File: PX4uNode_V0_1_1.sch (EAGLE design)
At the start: 129 parts, among them M3_MOUNT1101 MOUNT-HOLE3.1MM, M3_MOUNT1102 MOUNT-HOLE3.1MM, M3_MOUNT1103 MOUNT-HOLE3.1MM, M3_MOUNT1104 MOUNT-HOLE3.1MM, U101 STM32F4X7VX, U401 MAX3051, U402 MAX3051, X101 3.2x2.5 mm / 24 MHz / 15 ppm

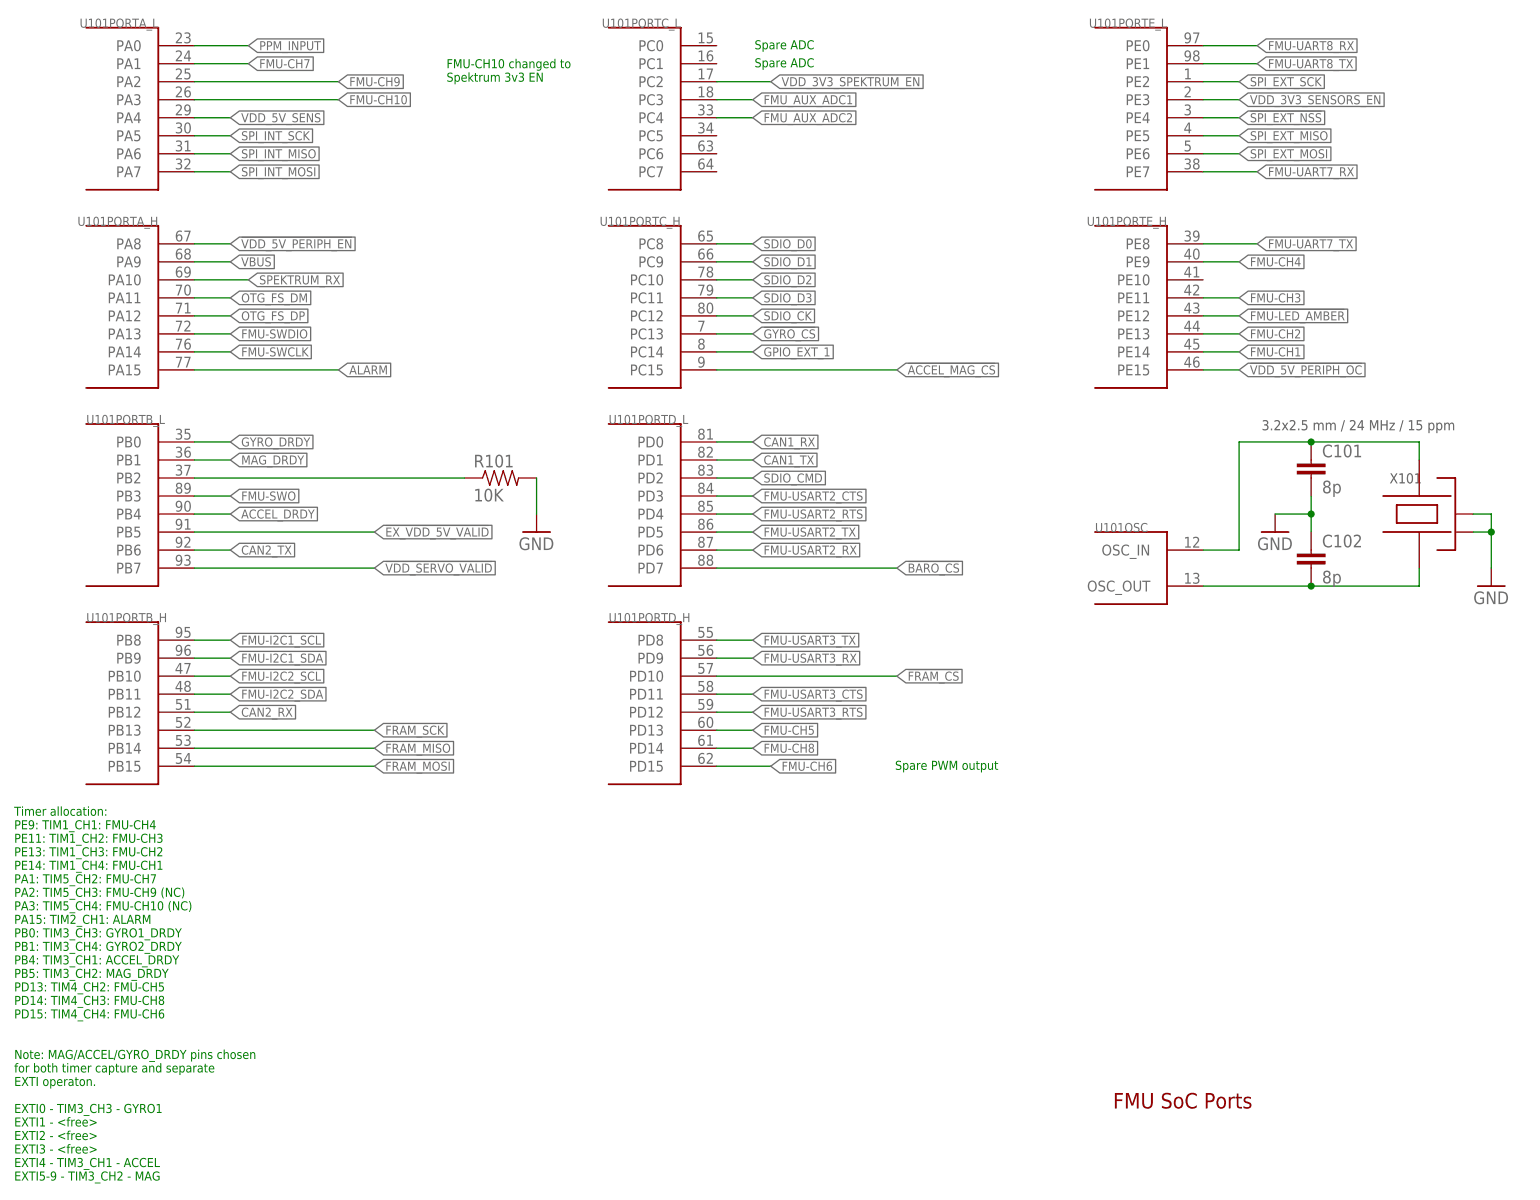
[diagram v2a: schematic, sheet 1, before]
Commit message: uNode - More pullup resistor placed
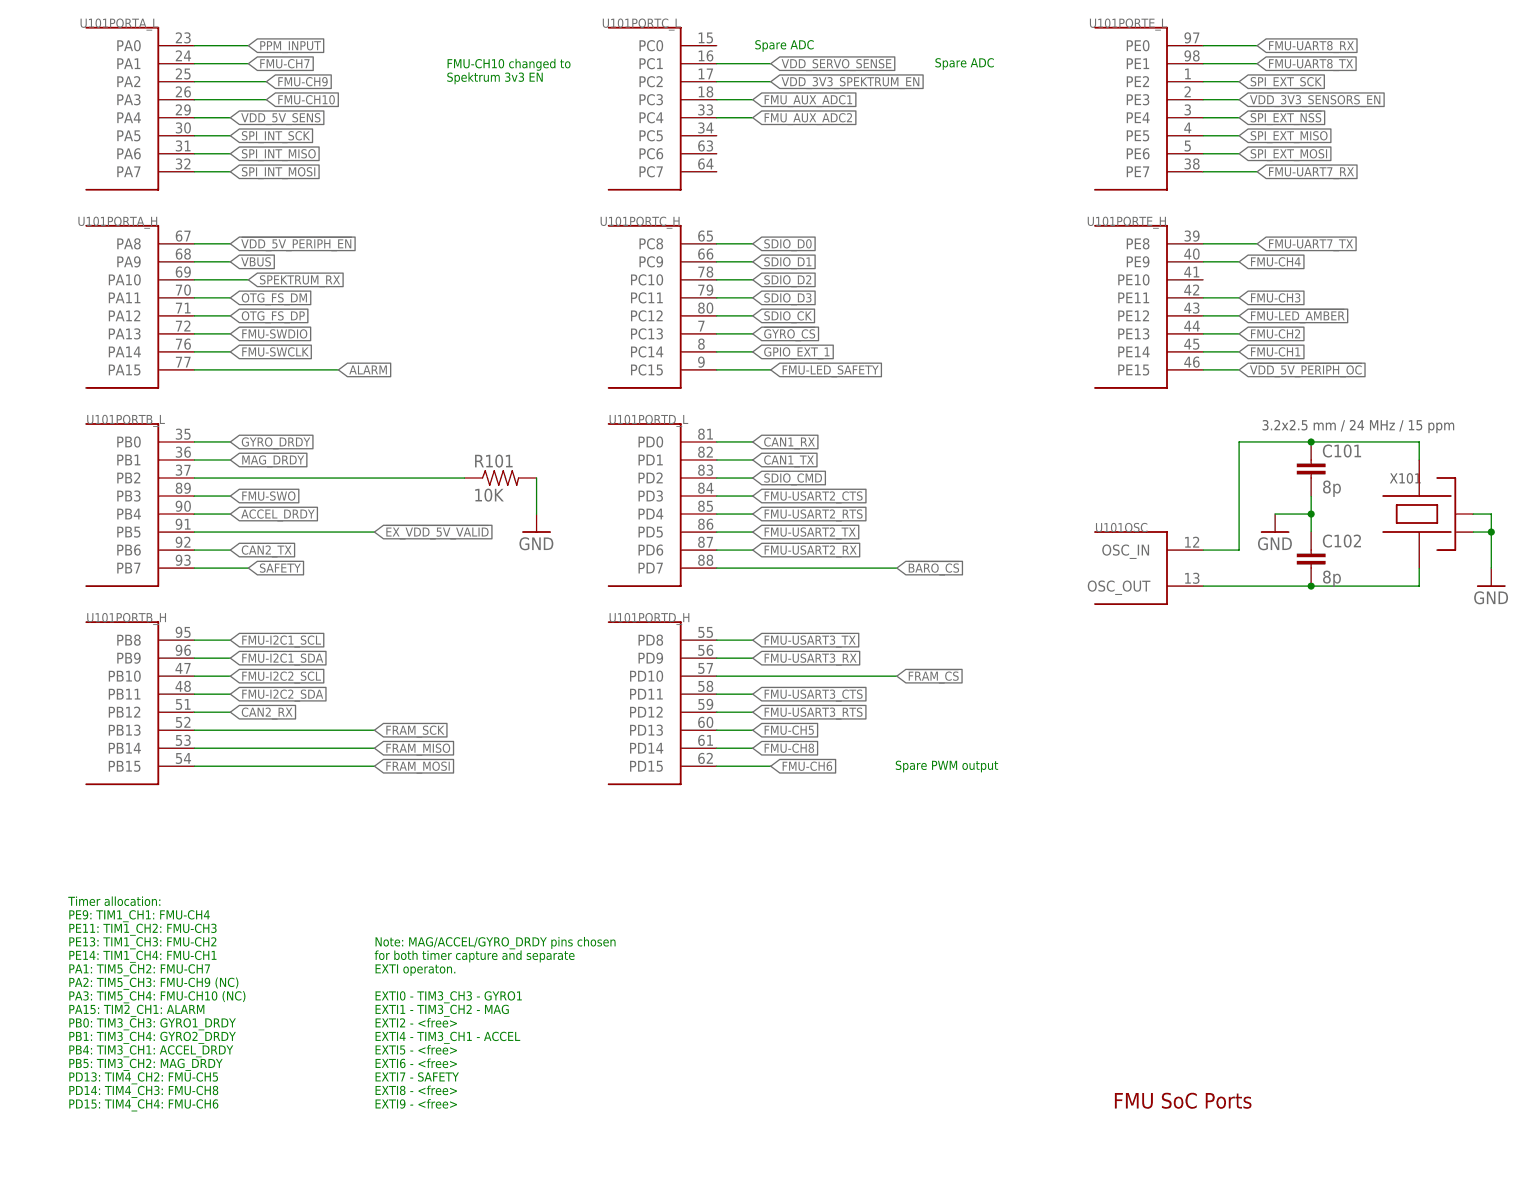
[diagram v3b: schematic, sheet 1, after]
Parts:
- added R1: 10K, pixhawk2:RESISTOR0402-RES
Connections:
- removed net !ACCEL_MAG_CS: U101PORTC_H.PC15
- removed net !VDD_SERVO_VALID: U101PORTB_L.PB7
- removed net VDD_SERVO_SENS: R902.1, R903.2
- new net VDD_SERVO_SENSE: R902.1, R903.2, U101PORTC_L.PC1
- net !VDD_5V_PERIPH_OC: now also R1.2
- net FMU-LED_SAFETY: now also U101PORTC_H.PC15
- net FMU-VDD_3V3: now also R1.1, R705.1
- net SAFETY: now also U101PORTB_L.PB7
- net VDD_5V: no longer R705.1
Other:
- note added: "Note: MAG/ACCEL/GYRO_DRDY pins chosen for both timer capture and separate EXTI operaton. EXTI0 - TIM3_CH3 - GYRO1 EXTI1 - TIM3_CH2 - MAG EXTI2 - <free> EXTI4 - TIM3_CH1 - ACCEL EXTI5 - <free> EXTI6 - <free> EXTI7 - SAFETY EXTI8 - <free> EXTI9 - <free>"
- note removed: "Note: MAG/ACCEL/GYRO_DRDY pins chosen for both timer capture and separate EXTI operaton. EXTI0 - TIM3_CH3 - GYRO1 EXTI1 - <free> EXTI2 - <free> EXTI3 - <free> EXTI4 - TIM3_CH1 - ACCEL EXTI5-9 - TIM3_CH2 - MAG"
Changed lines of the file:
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@@
 <part name="GND19" library="pixhawk2" deviceset="GND" device=""/>
 <part name="U$3" library="PX4lite" deviceset="NUF2042XV6" device=""/>
+<part name="R1" library="pixhawk2" deviceset="RESISTOR" device="0402-RES" value="10K">
+<attribute name="PARTNO" value="RC0402FR-0710KL"/>
+</part>
 </parts>
 <sheets>
@@
 <text x="162.56" y="15.24" size="2.1844" layer="94" font="vector" ratio="10">FMU SoC Ports
 </text>
-<text x="7.62" y="5.08" size="1.27" layer="91">Note: MAG/ACCEL/GYRO_DRDY pins chosen
+<text x="58.42" y="15.24" size="1.27" layer="91">Note: MAG/ACCEL/GYRO_DRDY pins chosen
 for both timer capture and separate
 EXTI operaton.
 EXTI0 - TIM3_CH3 - GYRO1
-EXTI1 - &lt;free&gt;
+EXTI1 - TIM3_CH2 - MAG
 EXTI2 - &lt;free&gt;
-EXTI3 - &lt;free&gt;
 EXTI4 - TIM3_CH1 - ACCEL
-EXTI5-9 - TIM3_CH2 - MAG
+EXTI5 - &lt;free&gt;
+EXTI6 - &lt;free&gt;
+EXTI7 - SAFETY
+EXTI8 - &lt;free&gt;
+EXTI9 - &lt;free&gt;
 </text>
-<text x="7.62" y="27.94" size="1.27" layer="91">Timer allocation:
+<text x="15.24" y="15.24" size="1.27" layer="91">Timer allocation:
 PE9: TIM1_CH1: FMU-CH4
 PE11: TIM1_CH2: FMU-CH3
@@
 <text x="131.826" y="62.992" size="1.27" layer="91">Spare PWM output</text>
 <text x="112.014" y="164.592" size="1.27" layer="91">Spare ADC</text>
-<text x="112.014" y="162.052" size="1.27" layer="91">Spare ADC</text>
+<text x="137.414" y="162.052" size="1.27" layer="91">Spare ADC</text>
 <text x="68.58" y="160.02" size="1.27" layer="91">FMU-CH10 changed to
 Spektrum 3v3 EN</text>
@@
 </segment>
 </net>
-<net name="!ACCEL_MAG_CS" class="0">
+<net name="FMU-LED_SAFETY" class="0">
 <segment>
 <pinref part="U101" gate="PORTC_H" pin="PC15"/>
-<wire x1="106.68" y1="119.38" x2="132.08" y2="119.38" width="0.1524" layer="91"/>
-<label x="132.08" y="119.38" size="1.27" layer="95" xref="yes"/>
+<wire x1="106.68" y1="119.38" x2="114.3" y2="119.38" width="0.1524" layer="91"/>
+<label x="114.3" y="119.38" size="1.27" layer="95" xref="yes"/>
 </segment>
 </net>
@@
 </segment>
 </net>
-<net name="!VDD_SERVO_VALID" class="0">
-<segment>
-<pinref part="U101" gate="PORTB_L" pin="PB7"/>
-<wire x1="33.02" y1="91.44" x2="58.42" y2="91.44" width="0.1524" layer="91"/>
-<label x="58.42" y="91.44" size="1.27" layer="95" xref="yes"/>
-</segment>
-</net>
 <net name="GPIO_EXT_1" class="0">
 <segment>
@@
 <segment>
 <pinref part="U101" gate="PORTA_L" pin="PA2"/>
-<wire x1="33.02" y1="160.02" x2="53.34" y2="160.02" width="0.1524" layer="91"/>
-<label x="53.34" y="160.02" size="1.27" layer="95" xref="yes"/>
+<wire x1="33.02" y1="160.02" x2="43.18" y2="160.02" width="0.1524" layer="91"/>
+<label x="43.18" y="160.02" size="1.27" layer="95" xref="yes"/>
 </segment>
 </net>
@@
 <segment>
 <pinref part="U101" gate="PORTA_L" pin="PA3"/>
-<wire x1="33.02" y1="157.48" x2="53.34" y2="157.48" width="0.1524" layer="91"/>
-<label x="53.34" y="157.48" size="1.27" layer="95" xref="yes"/>
+<wire x1="33.02" y1="157.48" x2="43.18" y2="157.48" width="0.1524" layer="91"/>
+<label x="43.18" y="157.48" size="1.27" layer="95" xref="yes"/>
+</segment>
+</net>
+<net name="SAFETY" class="0">
+<segment>
+<pinref part="U101" gate="PORTB_L" pin="PB7"/>
+<wire x1="33.02" y1="91.44" x2="40.64" y2="91.44" width="0.1524" layer="91"/>
+<label x="40.64" y="91.44" size="1.27" layer="95" xref="yes"/>
+</segment>
+</net>
+<net name="VDD_SERVO_SENSE" class="0">
+<segment>
+<pinref part="U101" gate="PORTC_L" pin="PC1"/>
+<wire x1="106.68" y1="162.56" x2="114.3" y2="162.56" width="0.1524" layer="91"/>
+<label x="114.3" y="162.56" size="1.27" layer="95" xref="yes"/>
 </segment>
 </net>
@@
 </instance>
 <instance part="D2" gate="G$1" x="205.74" y="127" rot="R270"/>
+<instance part="R1" gate="G$1" x="139.7" y="50.8" rot="R270">
+<attribute name="PARTNO" x="139.7" y="50.8" size="1.778" layer="96" rot="R90" display="off"/>
+</instance>
 </instances>
 <busses>
@@
 <junction x="45.72" y="116.84"/>
 </segment>
+<segment>
+<label x="86.36" y="68.58" size="1.27" layer="95" rot="R180" xref="yes"/>
+<pinref part="R705" gate="G$1" pin="1"/>
+<wire x1="129.54" y1="55.88" x2="129.54" y2="68.58" width="0.1524" layer="91"/>
+<wire x1="129.54" y1="68.58" x2="86.36" y2="68.58" width="0.1524" layer="91"/>
+<pinref part="R1" gate="G$1" pin="1"/>
+<wire x1="139.7" y1="55.88" x2="139.7" y2="68.58" width="0.1524" layer="91"/>
+<wire x1="139.7" y1="68.58" x2="129.54" y2="68.58" width="0.1524" layer="91"/>
+<junction x="129.54" y="68.58"/>
+</segment>
 </net>
 <net name="FMU-BOOT0" class="0">
@@
 <segment>
 <pinref part="U$703" gate="G$1" pin="IN"/>
-<wire x1="93.98" y1="60.96" x2="91.44" y2="60.96" width="0.1524" layer="91"/>
 <label x="86.36" y="60.96" size="1.27" layer="95" rot="R180" xref="yes"/>
-<pinref part="R705" gate="G$1" pin="1"/>
-<wire x1="91.44" y1="60.96" x2="86.36" y2="60.96" width="0.1524" layer="91"/>
-<wire x1="129.54" y1="55.88" x2="129.54" y2="68.58" width="0.1524" layer="91"/>
-<wire x1="129.54" y1="68.58" x2="91.44" y2="68.58" width="0.1524" layer="91"/>
-<wire x1="91.44" y1="68.58" x2="91.44" y2="60.96" width="0.1524" layer="91"/>
-<junction x="91.44" y="60.96"/>
+<wire x1="93.98" y1="60.96" x2="86.36" y2="60.96" width="0.1524" layer="91"/>
 </segment>
 <segment>
@@
 <segment>
 <wire x1="121.92" y1="35.56" x2="129.54" y2="35.56" width="0.1524" layer="91"/>
-<label x="134.62" y="35.56" size="1.27" layer="95" xref="yes"/>
+<label x="144.78" y="35.56" size="1.27" layer="95" xref="yes"/>
 <pinref part="U$703" gate="G$1" pin="!CE"/>
 <pinref part="R705" gate="G$1" pin="2"/>
-<wire x1="129.54" y1="35.56" x2="134.62" y2="35.56" width="0.1524" layer="91"/>
+<wire x1="129.54" y1="35.56" x2="144.78" y2="35.56" width="0.1524" layer="91"/>
 <wire x1="129.54" y1="45.72" x2="129.54" y2="35.56" width="0.1524" layer="91"/>
 <junction x="129.54" y="35.56"/>
@@
 <net name="VDD_5V_PERIPH" class="1">
 <segment>
-<wire x1="121.92" y1="60.96" x2="134.62" y2="60.96" width="0.1524" layer="91"/>
-<label x="134.62" y="60.96" size="1.27" layer="95" xref="yes"/>
+<wire x1="121.92" y1="60.96" x2="144.78" y2="60.96" width="0.1524" layer="91"/>
+<label x="144.78" y="60.96" size="1.27" layer="95" xref="yes"/>
 <pinref part="U$703" gate="G$1" pin="OUT"/>
 </segment>
@@
 <net name="!VDD_5V_PERIPH_OC" class="0">
 <segment>
-<label x="134.62" y="40.64" size="1.27" layer="95" xref="yes"/>
-<wire x1="121.92" y1="40.64" x2="134.62" y2="40.64" width="0.1524" layer="91"/>
+<label x="144.78" y="40.64" size="1.27" layer="95" xref="yes"/>
+<wire x1="121.92" y1="40.64" x2="139.7" y2="40.64" width="0.1524" layer="91"/>
 <pinref part="U$703" gate="G$1" pin="!FAULT"/>
+<pinref part="R1" gate="G$1" pin="2"/>
+<wire x1="139.7" y1="40.64" x2="144.78" y2="40.64" width="0.1524" layer="91"/>
+<wire x1="139.7" y1="45.72" x2="139.7" y2="40.64" width="0.1524" layer="91"/>
+<junction x="139.7" y="40.64"/>
 </segment>
 </net>
@@
 </segment>
 </net>
-<net name="VDD_SERVO_SENS" class="0">
+<net name="VDD_SERVO_SENSE" class="0">
 <segment>
 <pinref part="R903" gate="G$1" pin="2"/>

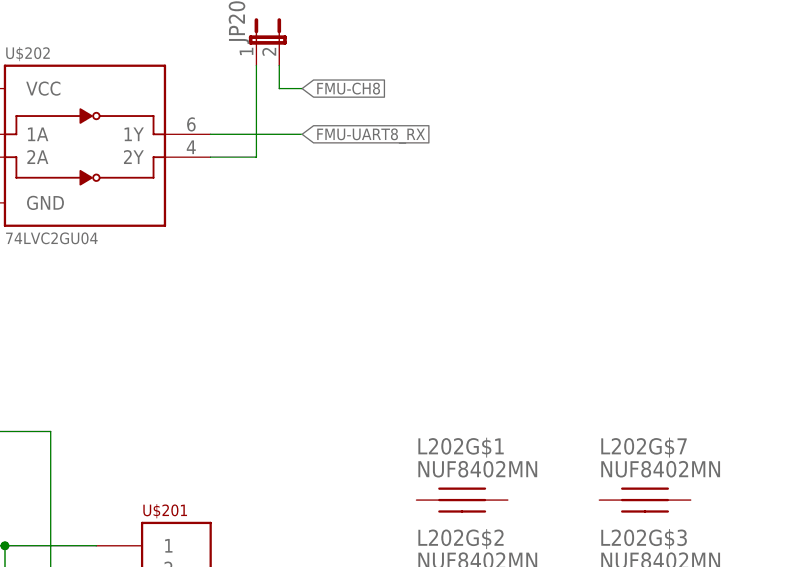
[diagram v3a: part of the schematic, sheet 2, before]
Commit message: PTH for boot and bat
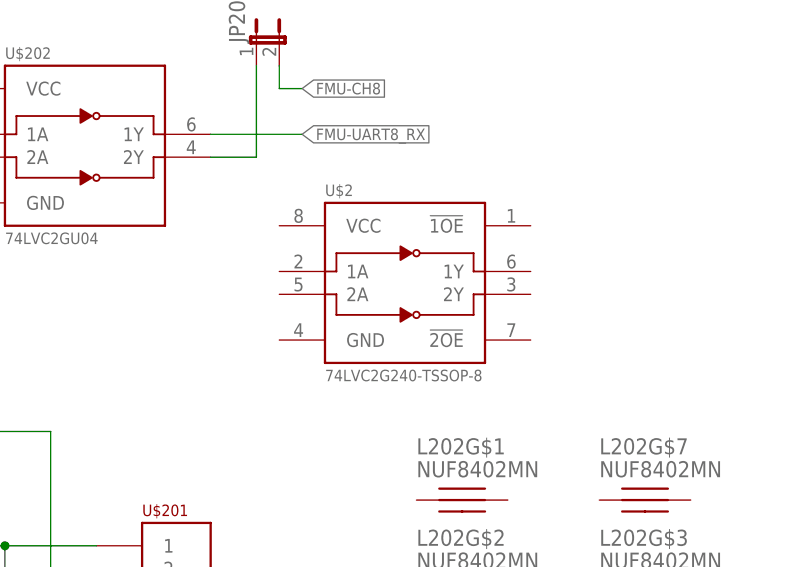
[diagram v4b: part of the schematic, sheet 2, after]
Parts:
- removed BOOT: PAD.04, pixhawk2:PAD.04
- removed JP701: M01SMD-4.5X1.5, SparkFun-Connectors:M01SMD-4.5X1.5
- added JP3, JP4: M01PTH, SparkFun-Connectors:M01PTH
- added U$2: 74LVC2G240-TSSOP-8, pixhawk2:74LVC2G240-TSSOP-8
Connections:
- net FMU-BOOT0: now also JP4.1; no longer BOOT.P$1
- net VBAT: now also JP3.1; no longer JP701.1
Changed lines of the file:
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@@
 </part>
 <part name="GND35" library="pixhawk2" deviceset="GND" device=""/>
-<part name="BOOT" library="pixhawk2" deviceset="PAD" device=".04">
-<attribute name="BOM" value="EXCLUDE"/>
-<attribute name="PARTNO" value="*"/>
-</part>
 <part name="R706" library="pixhawk2" deviceset="RESISTOR" device="0402-RES" value="1K">
 <attribute name="PARTNO" value="RC0402FR-071KL"/>
@@
 <attribute name="PARTNO" value="CC0402ZRY5V7BB104"/>
 </part>
-<part name="JP701" library="SparkFun-Connectors" deviceset="M01" device="SMD-4.5X1.5">
-<attribute name="BOM" value="EXCLUDE"/>
-</part>
 <part name="U$202" library="pixhawk2" deviceset="74LVC2GU04" device="">
 <attribute name="PARTNO" value="74LVC2GU04"/>
@@
 <attribute name="PARTNO" value="RC0402FR-0710KL"/>
 </part>
+<part name="JP3" library="SparkFun-Connectors" deviceset="M01" device="PTH"/>
+<part name="JP4" library="SparkFun-Connectors" deviceset="M01" device="PTH"/>
+<part name="U$2" library="pixhawk2" deviceset="74LVC2G240" device="-TSSOP-8"/>
 </parts>
 <sheets>
@@
 <instance part="GND19" gate="1" x="58.42" y="30.48"/>
 <instance part="U$3" gate="G$1" x="58.42" y="50.8"/>
+<instance part="U$2" gate="G$1" x="119.38" y="83.82"/>
 </instances>
 <busses>
@@
 <attribute name="PARTNO" x="170.18" y="157.48" size="1.778" layer="96" display="off"/>
 </instance>
-<instance part="JP701" gate="G$1" x="195.58" y="104.14">
-<attribute name="BOM" x="195.58" y="104.14" size="1.778" layer="96" display="off"/>
-</instance>
 <instance part="JP702" gate="G$1" x="195.58" y="91.44">
 <attribute name="BOM" x="195.58" y="91.44" size="1.778" layer="96" display="off"/>
@@
 <attribute name="PARTNO" x="139.7" y="50.8" size="1.778" layer="96" rot="R90" display="off"/>
 </instance>
+<instance part="JP3" gate="G$1" x="182.88" y="101.6"/>
 </instances>
 <busses>
@@
 <label x="185.42" y="111.76" size="1.27" layer="95" rot="R180" xref="yes"/>
 <pinref part="R706" gate="G$1" pin="1"/>
-<pinref part="JP701" gate="G$1" pin="1"/>
-<wire x1="203.2" y1="104.14" x2="213.36" y2="104.14" width="0.1524" layer="91"/>
-<wire x1="213.36" y1="104.14" x2="213.36" y2="111.76" width="0.1524" layer="91"/>
 <junction x="213.36" y="111.76"/>
+<pinref part="JP3" gate="G$1" pin="1"/>
+<wire x1="190.5" y1="101.6" x2="213.36" y2="101.6" width="0.1524" layer="91"/>
+<wire x1="213.36" y1="101.6" x2="213.36" y2="111.76" width="0.1524" layer="91"/>
 </segment>
 </net>
@@
 <attribute name="BOM" x="71.12" y="132.08" size="1.778" layer="96" display="off"/>
 </instance>
-<instance part="BOOT" gate="G$1" x="231.14" y="160.02">
-<attribute name="PARTNO" x="231.14" y="160.02" size="1.778" layer="96" display="off"/>
-<attribute name="BOM" x="231.14" y="160.02" size="1.778" layer="96" display="off"/>
-</instance>
 <instance part="JP1103" gate="G$1" x="20.32" y="17.78">
 <attribute name="PARTNO" x="20.32" y="17.78" size="1.778" layer="96" display="off"/>
@@
 <attribute name="BOM" x="15.24" y="12.7" size="1.778" layer="96" display="off"/>
 </instance>
+<instance part="JP4" gate="G$1" x="236.22" y="160.02" rot="R180"/>
 </instances>
 <busses>
@@
 <net name="FMU-BOOT0" class="0">
 <segment>
-<wire x1="223.52" y1="160.02" x2="215.9" y2="160.02" width="0.1524" layer="91"/>
 <label x="215.9" y="160.02" size="1.27" layer="95" rot="R180" xref="yes"/>
-<pinref part="BOOT" gate="G$1" pin="P$1"/>
+<pinref part="JP4" gate="G$1" pin="1"/>
+<wire x1="218.44" y1="160.02" x2="215.9" y2="160.02" width="0.1524" layer="91"/>
+<wire x1="228.6" y1="160.02" x2="218.44" y2="160.02" width="0.1524" layer="91"/>
 </segment>
 </net>
